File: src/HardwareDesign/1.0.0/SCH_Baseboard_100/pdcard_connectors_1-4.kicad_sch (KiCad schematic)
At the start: 12 parts, among them J4 10018784-10200TLF, J5 10018784-10200TLF, J6 10018784-10200TLF, J7 10018784-10200TLF

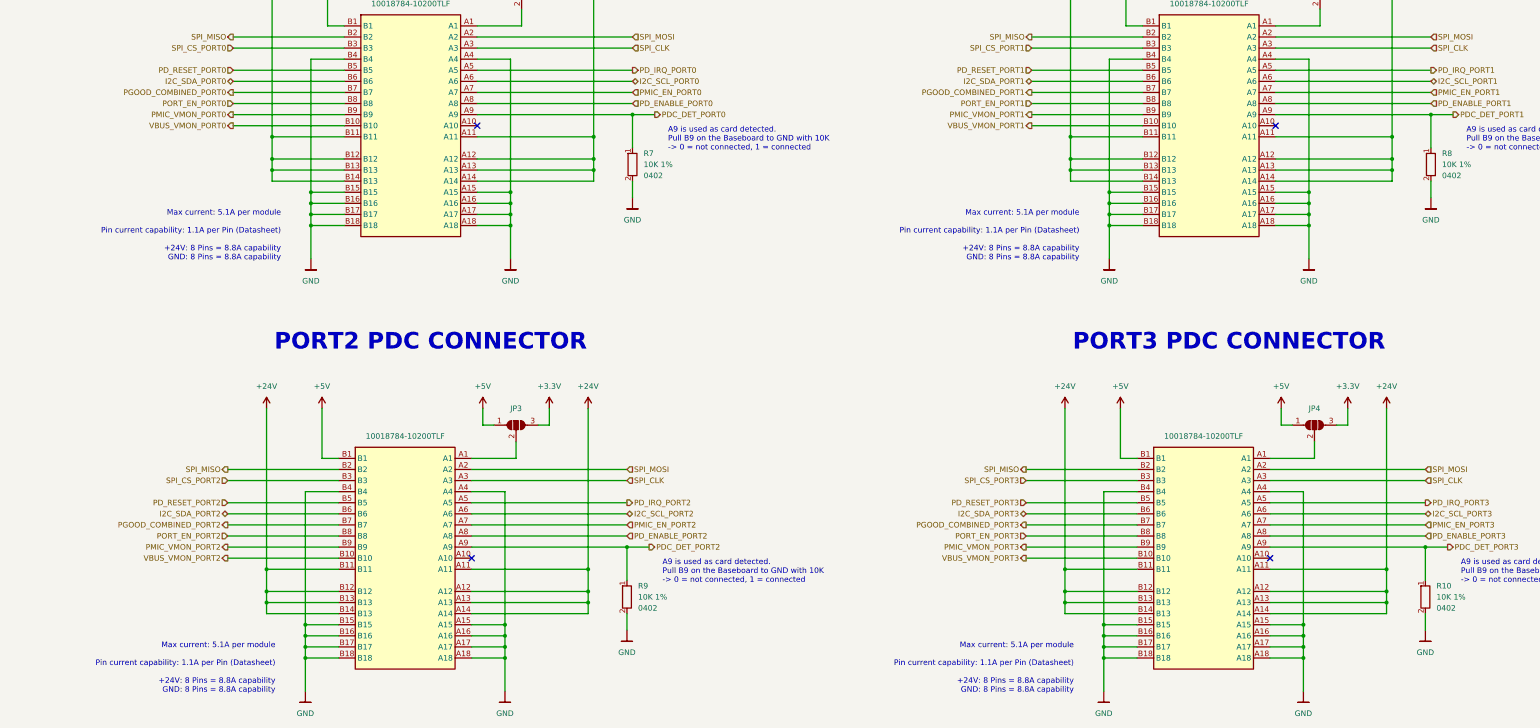
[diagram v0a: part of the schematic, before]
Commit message: Add bladecore to design
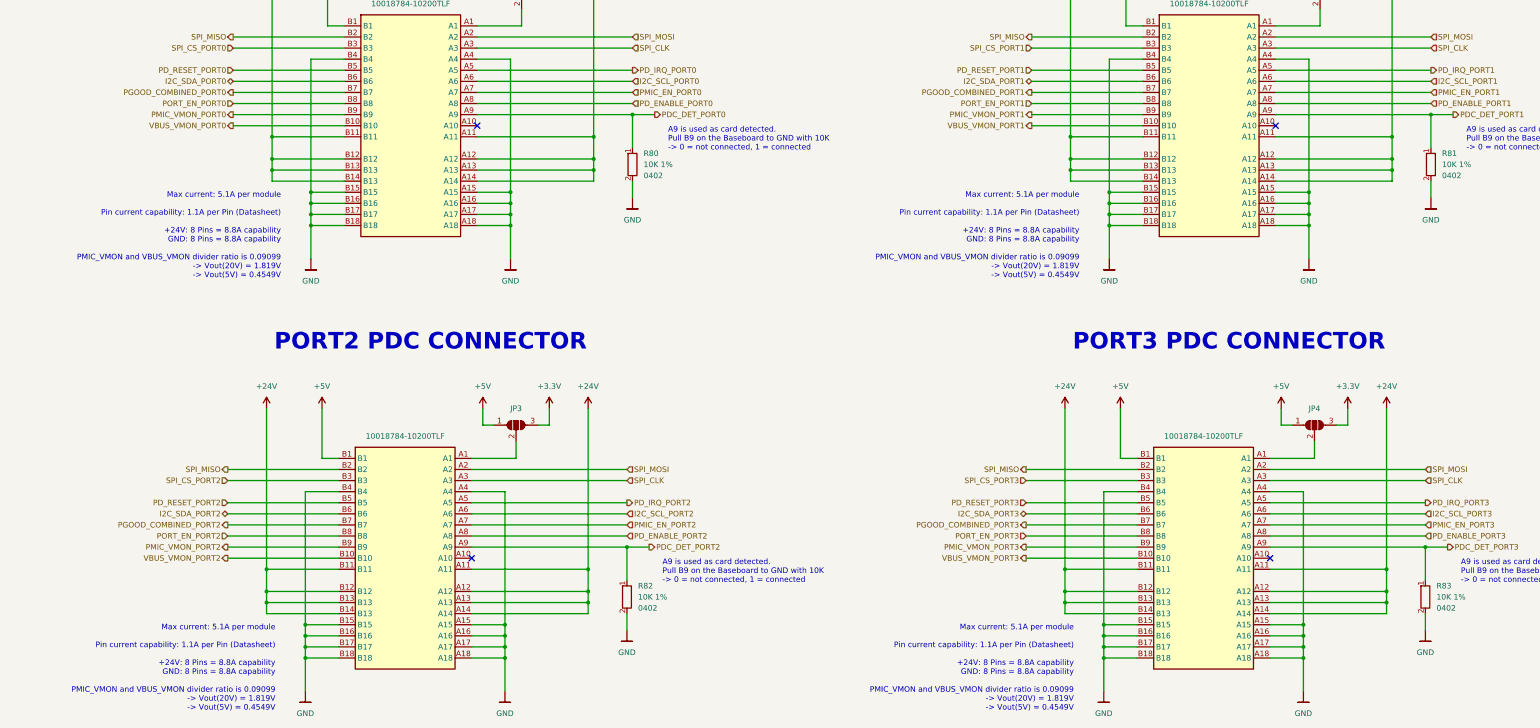
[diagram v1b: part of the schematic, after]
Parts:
- removed R10, R7, R8, R9: 10K 1%, Resistor_SMD:R_0402_1005Metric, symbol DS_Resistor_0402:10K 1% 0402
- added R80, R81, R82, R83: 10K 1%, Resistor_SMD:R_0402_1005Metric, symbol DS_Resistor_0402:10K 1% 0402
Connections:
- net GND: now also R80.2, R81.2, R82.2, R83.2
- net PDC_DET_PORT0: now also R80.1
- net PDC_DET_PORT1: now also R81.1
- net PDC_DET_PORT2: now also R82.1
- net PDC_DET_PORT3: now also R83.1
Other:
- note added: "Max current: 5.1A per module Pin current capability: 1.1A per Pin (Datasheet) +24V: 8 Pins = 8.8A capability GND: 8 Pins = 8.8A capability PMIC_VMON and VBUS_VMON divider ratio is 0.09099 -> Vout(20V) = 1.819V -> Vout(5V) = 0.4549V"
- note removed: "Max current: 5.1A per module Pin current capability: 1.1A per Pin (Datasheet) +24V: 8 Pins = 8.8A capability GND: 8 Pins = 8.8A capability"
